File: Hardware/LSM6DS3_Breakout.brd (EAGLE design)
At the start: 25.4 x 25.4 mm, 33 parts, among them U2 LSM6DS3DOT_INDICATION

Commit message: Swapped choke
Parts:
- L1: value NDUC-12579 -> RES-07859
- moved L1 67.3 mm to (-43.2, -30.5)
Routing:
- net 3.3V: track 60.4 -> 58.7 mm
- net N$1: track 7.93 -> 6.45 mm
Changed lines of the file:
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@@
 <attribute name="PROD_ID" value="CAP-08390" x="10.4775" y="15.5575" size="1.778" layer="27" display="off"/>
 </element>
-<element name="L1" library="SparkFun-Passives" package="0603" value="NDUC-12579" x="7.3025" y="13.97"/>
 <element name="SJ1" library="SparkFun-Passives" package="PAD-JUMPER-3-2OF3_NC_BY_PASTE_YES_SILK_FULL_BOX" value="I2C ADDR LSB" x="13.97" y="22.86"/>
 <element name="SJ2" library="SparkFun-Passives" package="PAD-JUMPER-2-NC_BY_PASTE_YES_SILK" value="" x="19.05" y="14.9225"/>
@@
 <element name="R2" library="SparkFun-Resistors" package="0603-RES" value="4.7K" x="1.905" y="5.23875" rot="R180">
 <attribute name="PROD_ID" value="RES-07857" x="1.905" y="5.23875" size="1.778" layer="27" rot="R180" display="off"/>
+</element>
+<element name="L1" library="SparkFun-Passives" package="0603" value="RES-07859" x="-43.18" y="-30.48">
+<attribute name="PROD_ID" value="RES-07859" x="-43.18" y="-30.48" size="1.778" layer="27" display="off"/>
 </element>
 </elements>
@@
 <signal name="N$1">
 <contactref element="C3" pad="1"/>
-<contactref element="L1" pad="2"/>
 <contactref element="U2" pad="8"/>
 <wire x1="11.525" y1="13.45" x2="10.045" y2="13.45" width="0.254" layer="1"/>
@@
 <wire x1="9.965625" y1="13.45" x2="9.9434" y2="13.45" width="0.254" layer="1"/>
 <wire x1="9.9434" y1="13.45" x2="9.5504" y2="13.843" width="0.254" layer="1"/>
-<wire x1="8.1525" y1="13.97" x2="8.1525" y2="15.455" width="0.4064" layer="1"/>
 <wire x1="8.1525" y1="15.455" x2="8.255" y2="15.5575" width="0.4064" layer="1"/>
+<contactref element="L1" pad="2"/>
+<wire x1="9.5504" y1="13.843" x2="-42.33" y2="-30.48" width="0" layer="19" extent="1-1"/>
 </signal>
 <signal name="SCL">
@@
 <contactref element="SJ6" pad="3"/>
 <contactref element="U2" pad="5"/>
-<contactref element="L1" pad="1"/>
 <wire x1="13.2" y1="14.47" x2="13.335" y2="14.605" width="0.254" layer="1"/>
 <wire x1="15.1375" y1="14.82" x2="14.9225" y2="14.605" width="0.4064" layer="1"/>
@@
 <wire x1="7.46125" y1="12.22375" x2="8.255" y2="12.22375" width="0.4064" layer="16"/>
 <wire x1="8.255" y1="12.22375" x2="8.255" y2="12.54125" width="0.4064" layer="16"/>
-<wire x1="6.4525" y1="13.97" x2="6.4525" y2="12.28" width="0.4064" layer="1"/>
 <wire x1="6.4525" y1="12.28" x2="6.50875" y2="12.22375" width="0.4064" layer="1"/>
 <wire x1="13.2" y1="14.47" x2="13.2" y2="14.5827125" width="0.254" layer="1"/>
@@
 <wire x1="5.87375" y1="11.7475" x2="6.35" y2="12.22375" width="0.254" layer="16"/>
 <wire x1="6.35" y1="12.22375" x2="7.46125" y2="12.22375" width="0.254" layer="16"/>
+<contactref element="L1" pad="1"/>
+<wire x1="1.055" y1="3.175" x2="-44.03" y2="-30.48" width="0" layer="19" extent="1-1"/>
 </signal>
 <signal name="N$2">

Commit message: Fixed ripped up component
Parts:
- moved L1 67.2 mm to (7.30, 13.8)
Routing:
- net N$1: track 6.45 -> 8.09 mm
- net 3.3V: track 58.7 -> 60.3 mm
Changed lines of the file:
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@@
 <attribute name="PROD_ID" value="RES-07857" x="1.905" y="5.23875" size="1.778" layer="27" rot="R180" display="off"/>
 </element>
-<element name="L1" library="SparkFun-Passives" package="0603" value="RES-07859" x="-43.18" y="-30.48">
-<attribute name="PROD_ID" value="RES-07859" x="-43.18" y="-30.48" size="1.778" layer="27" display="off"/>
+<element name="L1" library="SparkFun-Passives" package="0603" value="RES-07859" x="7.3025" y="13.81125">
+<attribute name="PROD_ID" value="RES-07859" x="7.3025" y="13.81125" size="1.778" layer="27" display="off"/>
 </element>
 </elements>
@@
 <wire x1="8.1525" y1="15.455" x2="8.255" y2="15.5575" width="0.4064" layer="1"/>
 <contactref element="L1" pad="2"/>
-<wire x1="9.5504" y1="13.843" x2="-42.33" y2="-30.48" width="0" layer="19" extent="1-1"/>
+<wire x1="8.1525" y1="13.81125" x2="8.1525" y2="15.455" width="0.4064" layer="1"/>
 </signal>
 <signal name="SCL">
@@
 <wire x1="6.35" y1="12.22375" x2="7.46125" y2="12.22375" width="0.254" layer="16"/>
 <contactref element="L1" pad="1"/>
-<wire x1="1.055" y1="3.175" x2="-44.03" y2="-30.48" width="0" layer="19" extent="1-1"/>
+<wire x1="6.4525" y1="13.81125" x2="6.4525" y2="12.28" width="0.4064" layer="1"/>
 </signal>
 <signal name="N$2">

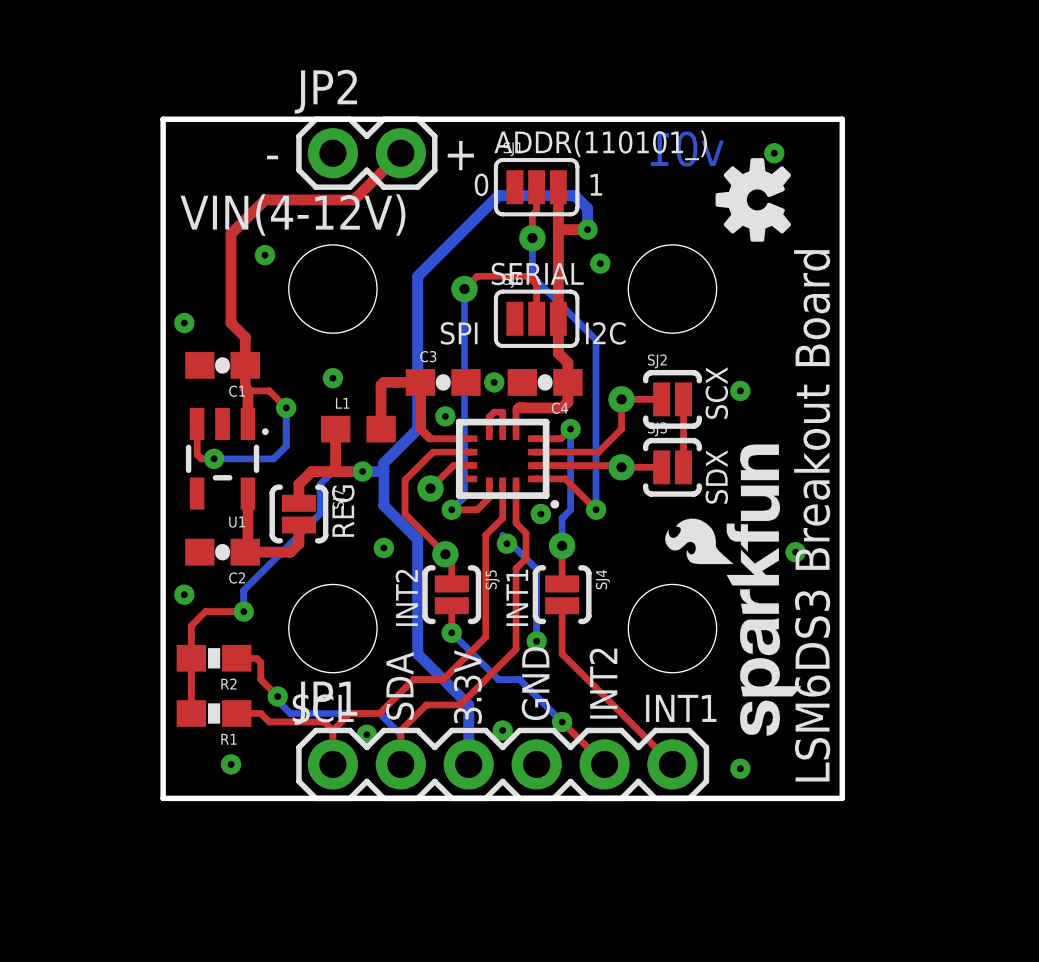
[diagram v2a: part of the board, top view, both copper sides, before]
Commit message: Switched pads for pins, grew board.
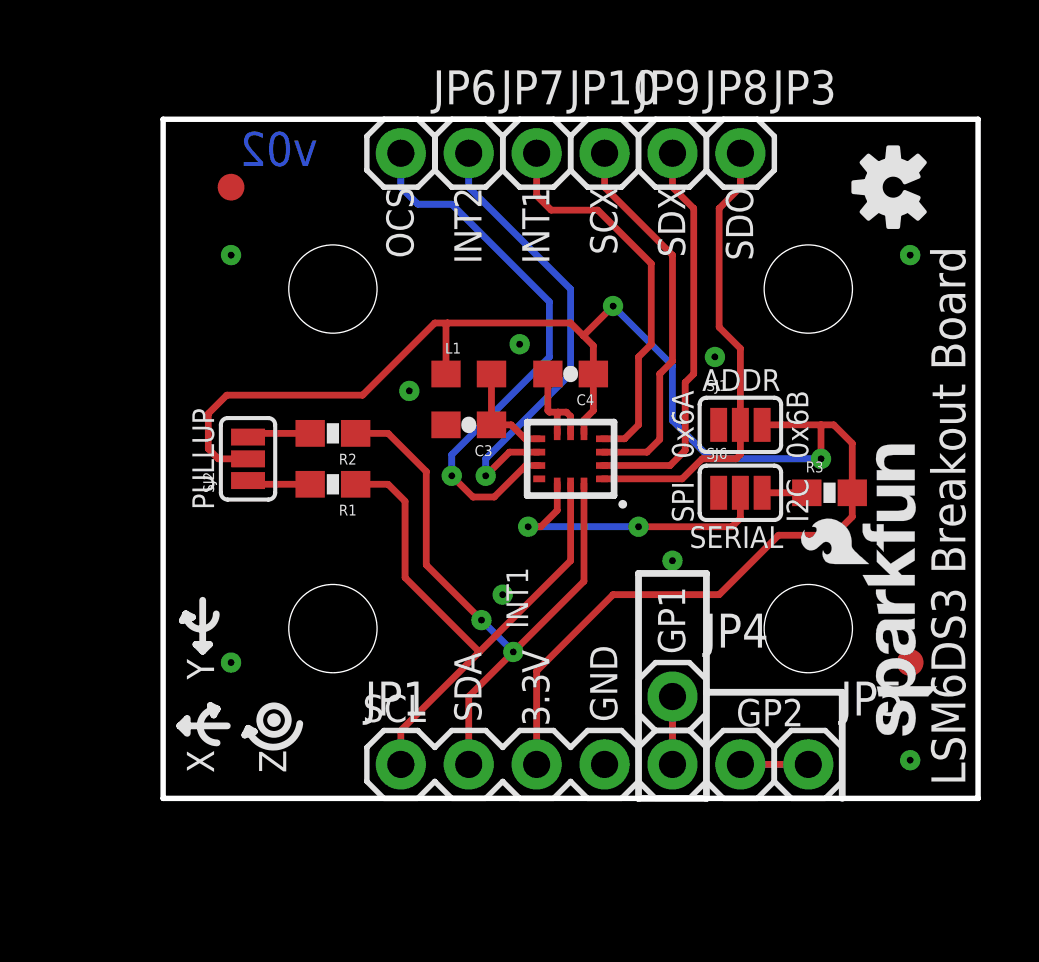
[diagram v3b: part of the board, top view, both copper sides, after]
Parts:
- removed C1, C2: 1.0uF, SparkFun-Capacitors:0603-CAP
- removed JP2: (no value), SparkFun-Connectors:1X02
- removed SJ3, SJ7: (no value), SparkFun-Passives:PAD-JUMPER-2-NC_BY_PASTE_YES_SILK
- removed SJ4: INT1_JP, SparkFun-Passives:PAD-JUMPER-2-NC_BY_PASTE_YES_SILK
- removed SJ5: INT2_JP, SparkFun-Passives:PAD-JUMPER-2-NC_BY_PASTE_YES_SILK
- removed TP1: SCX_TP, SparkFun-Passives:TP_15TH
- removed TP2: SDX_TP, SparkFun-Passives:TP_15TH
- removed TP3: OCS_TP, SparkFun-Passives:TP_15TH
- removed TP4: SD0_TP, SparkFun-Passives:TP_15TH
- removed TP5: CS_TP, SparkFun-Passives:TP_15TH
- removed TP6: INT2_TP, SparkFun-Passives:TP_15TH
- removed TP7: INT1_TP, SparkFun-Passives:TP_15TH
- removed U1: (no value), SparkFun-PowerIC:SOT23-5
- added FID1, FID2: FIDUCIAL1X2, SparkFun-Aesthetics:FIDUCIAL-1X2
- added JP10: INT1, SparkFun-Connectors:1X01
- added JP3: SDO, SparkFun-Connectors:1X01
- added JP4: GP1, SparkFun-Connectors:1X01
- added JP5: GP2, SparkFun-Connectors:1X01
- added JP6: OCS, SparkFun-Connectors:1X01
- added JP7: INT2, SparkFun-Connectors:1X01
- added JP8: SDx, SparkFun-Connectors:1X01
- added JP9: SCx, SparkFun-Connectors:1X01
- added R3: 4.7K, SparkFun-Resistors:0603-RES
- JP1: value (none) -> IO
- LOGO3: value SFE_LOGO_FLAME.4_INCH -> SFE_LOGO_FLAME.6_INCH; device SparkFun-Aesthetics:SFE_LOGO_FLAME_.4 -> SparkFun-Aesthetics:SFE_LOGO_FLAME_.6
- SJ2: value (none) -> S_MODE; device SparkFun-Passives:PAD-JUMPER-2-NC_BY_PASTE_YES_SILK -> SparkFun-Passives:PAD-JUMPER-3-NC_BY_PASTE_YES_SILK_FULL_BOX
- moved LOGO3 16.6 mm to (21.6, 18.4), turned to 270 degrees
- moved SJ2 16.0 mm to (3.17, 12.7), turned to 90 degrees
- moved SJ1 11.7 mm to (21.6, 14.0)
- moved SJ6 10.0 mm to (21.6, 11.4)
- moved R1 9.66 mm to (6.35, 11.7)
- moved R2 9.52 mm to (6.35, 13.7)
- moved LOGO2 5.10 mm to (27.3, 22.9)
- moved LOGO1 5.08 mm to (29.1, 1.91)
- moved STANDOFF3 5.08 mm to (24.1, 19.1)
- moved STANDOFF4 5.08 mm to (24.1, 6.35)
- moved L1 4.61 mm to (11.4, 15.9)
- moved JP1 2.54 mm to (8.89, 1.27)
- moved U2 2.54 mm to (15.2, 12.7)
- moved C3 1.85 mm to (11.4, 14.0), turned to 180 degrees
- moved C4 1.00 mm to (15.2, 15.9)
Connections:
- new net N$7: R3.1, SJ6.3
- net 3.3V: now also R3.2, SJ2.2; no longer R1.2, R2.2, SJ6.3, SJ7.1
- net CS: no longer TP5.P$1
- net GND: no longer C1.2, C2.2, JP2.1, SJ2.2, SJ3.2, U1.2
- net INT1: now also JP10.1; no longer SJ4.1, TP7.P$1
- net INT2: now also JP7.1; no longer SJ5.1, TP6.P$1
- net N$2: now also JP6.1; no longer TP3.P$1
- net N$3: now also JP4.1; no longer SJ5.2
- net N$4: now also JP5.1; no longer SJ4.2
- net N$5: now also R1.2, SJ2.1; no longer C1.1, JP2.2, U1.1, U1.3
- net N$6: now also R2.2, SJ2.3; no longer C2.1, SJ7.2, U1.5
- net SCX: now also JP9.1; no longer SJ2.1, TP1.P$1
- net SDO/SA0: now also JP3.1; no longer TP4.P$1
- net SDX: now also JP8.1; no longer SJ3.1, TP2.P$1
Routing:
- net N$5: track 22.8 -> 2.38 mm, vias 2 -> 0
- net N$2: track 1.88 -> 20.7 mm, vias 0 -> 1
- net SDX: track 4.80 -> 14.9 mm
- net INT2: track 7.52 -> 17.3 mm, vias 0 -> 1
- net SCX: track 6.24 -> 14.3 mm
- net INT1: track 7.44 -> 14.7 mm, vias 1 -> 0
- net GND: track 9.07 -> 3.81 mm, vias 18 -> 9
- net N$1: track 8.09 -> 3.91 mm
- net SCL: track 18.3 -> 22.0 mm
- net N$3: track 8.77 -> 5.08 mm, vias 2 -> 0
- net CS: track 14.9 -> 11.4 mm, vias 1 -> 2
- net N$6: track 5.07 -> 2.38 mm
- net N$4: track 7.65 -> 5.08 mm
- net 3.3V: track 60.3 -> 62.8 mm, vias 3 -> 2
- net N$7: track 0.00 -> 1.67 mm
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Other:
- board size 25.4 x 25.4 mm -> 30.5 x 25.4 mm
- board text added: "0x6A"
- board text added: "0x6B"
- board text added: "ADDR"
- board text added: "GP1"
- board text added: "GP2"
- board text added: "OCS"
- board text added: "PULLUP"
- board text added: "SDO"
- board text added: "X"
- board text added: "Y"
- board text added: "Z"
- board text added: "v02"
- board text removed: "+"
- board text removed: "-"
- board text removed: "0"
- board text removed: "1"
- board text removed: "ADDR(110101_)"
- board text removed: "REG"
- board text removed: "VIN(4-12V)"
- board text removed: "v01"

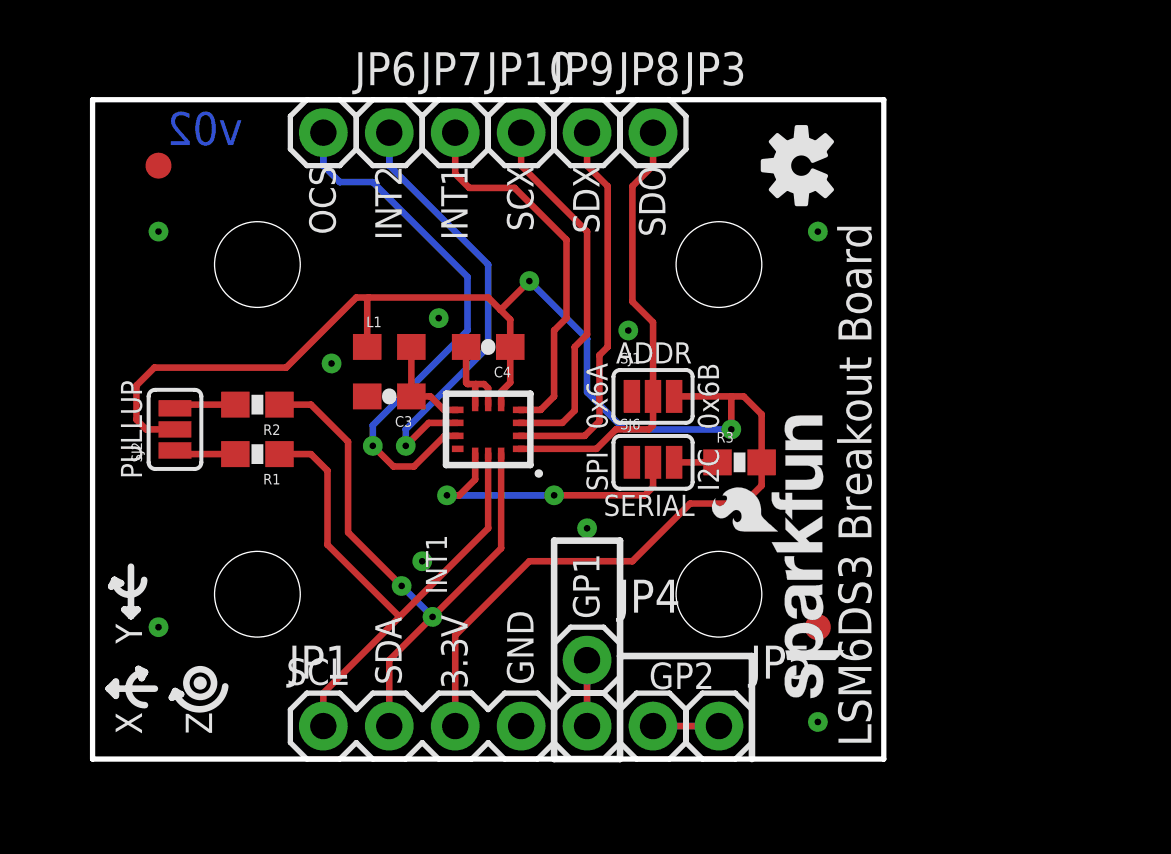
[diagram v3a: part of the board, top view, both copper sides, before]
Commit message: Corrected QC suggestions
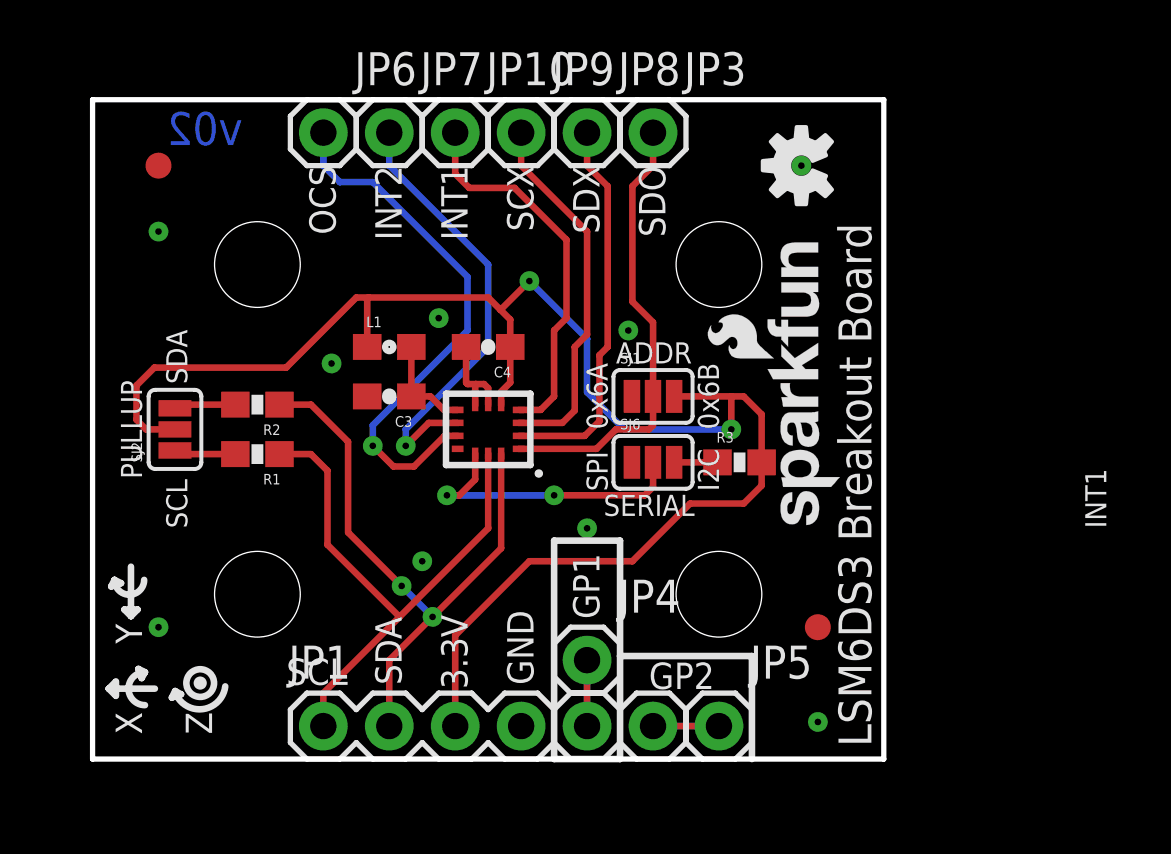
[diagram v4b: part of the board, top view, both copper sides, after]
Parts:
- moved LOGO1 6.67 mm to (28.9, 8.57)
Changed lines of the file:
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@@
 <text x="21.43125" y="2.69875" size="1.016" layer="21" font="vector" ratio="15">GP2</text>
 <text x="1.905" y="10.795" size="0.8128" layer="21" font="vector" ratio="15" rot="R90">PULLUP</text>
-<text x="13.6525" y="6.35" size="0.8128" layer="21" font="vector" ratio="15" rot="R90">INT1</text>
+<text x="39.0525" y="8.89" size="0.8128" layer="21" font="vector" ratio="15" rot="R90">INT1</text>
 <text x="19.685" y="9.36625" size="0.8128" layer="21" font="vector" ratio="15">SERIAL</text>
 <text x="20.16125" y="15.24" size="0.8128" layer="21" font="vector" ratio="15">ADDR</text>
@@
 <text x="19.52625" y="22.86" size="1.016" layer="22" font="vector" ratio="15" rot="MR270">SDX</text>
 <text x="22.06625" y="22.86" size="1.016" layer="22" font="vector" ratio="15" rot="MR270">SDO</text>
+<text x="3.65125" y="14.44625" size="0.8128" layer="21" font="vector" ratio="15" rot="R90">SDA</text>
+<text x="3.65125" y="8.89" size="0.8128" layer="21" font="vector" ratio="15" rot="R90">SCL</text>
 </plain>
 <attributes>
@@
 <attribute name="PROD_ID" value="CAP-08390" x="15.24" y="15.875" size="1.778" layer="27" rot="R180" display="off"/>
 </element>
-<element name="LOGO1" library="SparkFun-Aesthetics" package="SFE_LOGO_NAME_FLAME_.1" value="SFE_LOGO_NAME_FLAME.1_INCH" x="29.05125" y="1.905" rot="R90"/>
+<element name="LOGO1" library="SparkFun-Aesthetics" package="SFE_LOGO_NAME_FLAME_.1" value="SFE_LOGO_NAME_FLAME.1_INCH" x="28.8925" y="8.5725" rot="R90"/>
 <element name="LOGO2" library="SparkFun-Aesthetics" package="OSHW-LOGO-S" value="OSHW-LOGOS" x="27.305" y="22.86" rot="R90"/>
 <element name="LOGO3" library="SparkFun-Aesthetics" package="SFE_LOGO_FLAME_.6" value="SFE_LOGO_FLAME.6_INCH" x="21.59" y="18.415" rot="MR270"/>
@@
 <via x="2.54" y="5.08" extent="1-16" drill="0.254"/>
 <via x="2.54" y="20.32" extent="1-16" drill="0.254"/>
-<via x="27.94" y="20.32" extent="1-16" drill="0.254"/>
+<via x="27.305" y="22.86" extent="1-16" drill="0.254"/>
 <via x="27.94" y="1.42875" extent="1-16" drill="0.254"/>
 <via x="12.7" y="7.62" extent="1-16" drill="0.254"/>
